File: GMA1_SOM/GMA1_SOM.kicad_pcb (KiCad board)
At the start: 6 copper layers, 67.6 x 25.4 mm, 8 parts, among them J1 USB4105-GF-A, J2 SODIMM-200_Split, U1 CCGM1A1, U2 RP2040, U3 LAN8742A-CZ-TR, U4 LAN8742A-CZ-TR, Y1 SG-210STF 25.0000ML0, Y2 SG-210STF 25.0000ML0

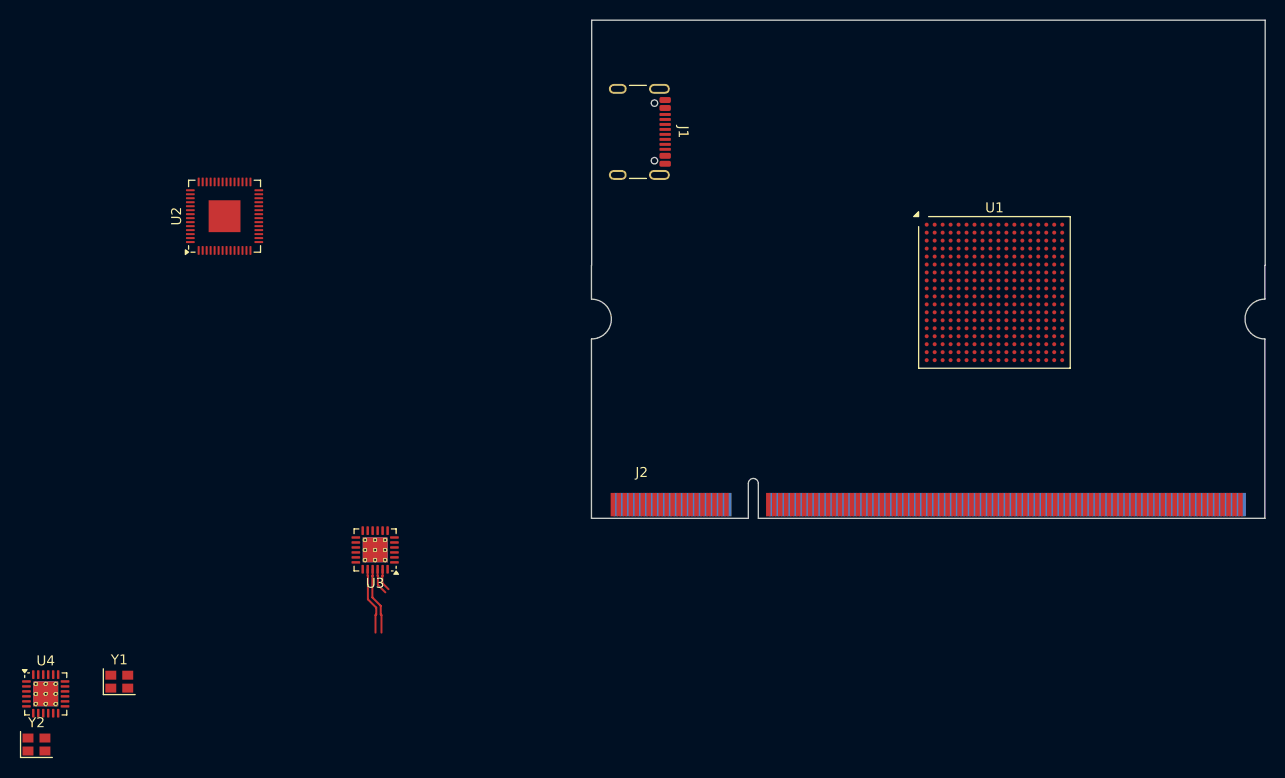
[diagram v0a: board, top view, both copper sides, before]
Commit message: add display and ram
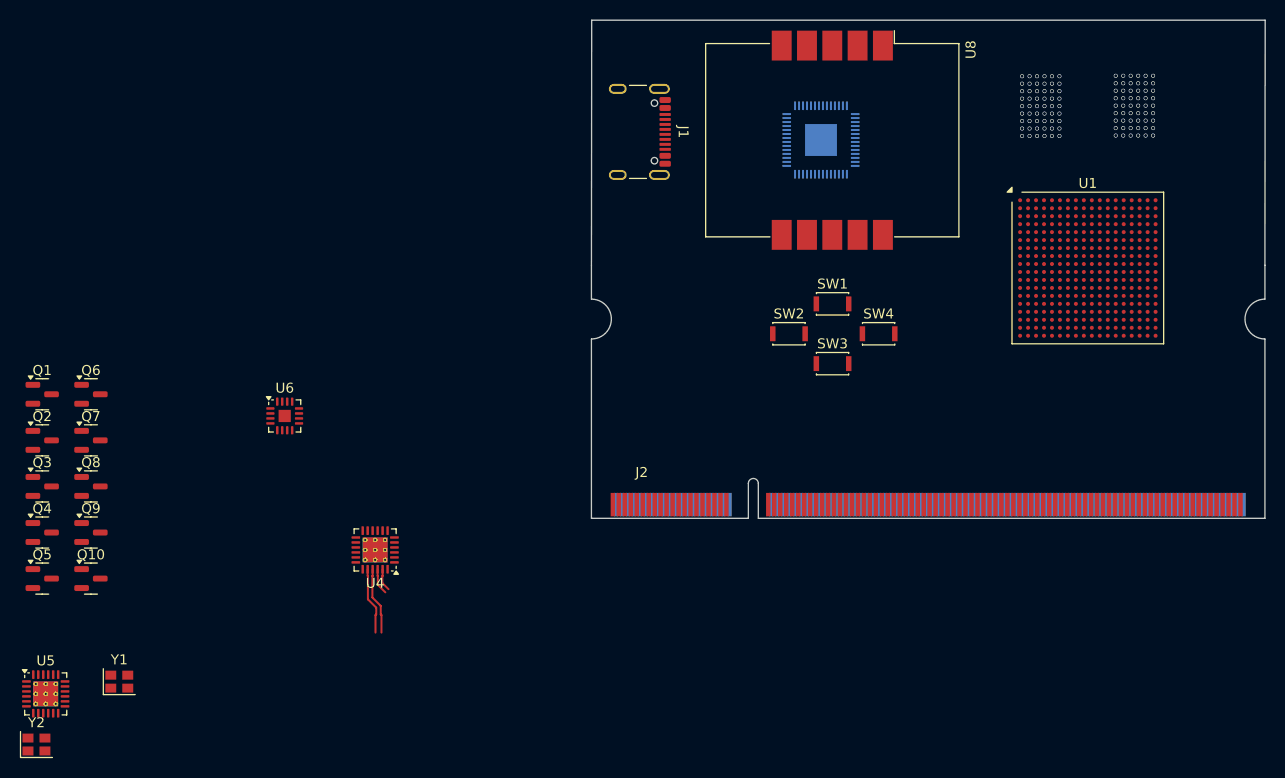
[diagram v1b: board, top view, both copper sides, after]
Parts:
- added Q1: BSS138, Package_TO_SOT_SMD:SOT-23, F.Cu at (135.0, 121.1)
- added Q10: BSS138, Package_TO_SOT_SMD:SOT-23, F.Cu at (139.9, 139.6)
- added Q2: BSS138, Package_TO_SOT_SMD:SOT-23, F.Cu at (135.0, 125.7)
- added Q3: BSS138, Package_TO_SOT_SMD:SOT-23, F.Cu at (135.0, 130.3)
- added Q4: BSS138, Package_TO_SOT_SMD:SOT-23, F.Cu at (135.0, 134.9)
- added Q5: BSS138, Package_TO_SOT_SMD:SOT-23, F.Cu at (135.0, 139.6)
- added Q6: BSS138, Package_TO_SOT_SMD:SOT-23, F.Cu at (139.9, 121.1)
- added Q7: BSS138, Package_TO_SOT_SMD:SOT-23, F.Cu at (139.9, 125.7)
- added Q8: BSS138, Package_TO_SOT_SMD:SOT-23, F.Cu at (139.9, 130.3)
- added Q9: BSS138, Package_TO_SOT_SMD:SOT-23, F.Cu at (139.9, 134.9)
- added SW1: KXT 331 LHS, Button_Switch_SMD:SW_SPST_CK_KXT3, F.Cu at (214.4, 112.0)
- added SW2: KXT 331 LHS, Button_Switch_SMD:SW_SPST_CK_KXT3, F.Cu at (210.0, 115.0)
- added SW3: KXT 331 LHS, Button_Switch_SMD:SW_SPST_CK_KXT3, F.Cu at (214.4, 118.0)
- added SW4: KXT 331 LHS, Button_Switch_SMD:SW_SPST_CK_KXT3, F.Cu at (219.0, 115.0)
- added U3: IS66WVC2M16EALL-7010BLI, Project_Library:BGA-54_6x9_6.0x8.0mm, B.Cu at (235.3, 92.2)
- added U6: MAX98357B, Package_DFN_QFN:TQFN-16-1EP_3x3mm_P0.5mm_EP1.23x1.23mm, F.Cu at (159.4, 123.2)
- added U7: IS66WVC2M16EALL-7010BLI, Project_Library:BGA-54_6x9_6.0x8.0mm, B.Cu at (244.7, 92.1)
- added U8: HDSM-543B, Display:HDSM-541B_HDSM-543B, F.Cu at (214.3, 95.6)
- U2: moved to B.Cu
- moved U2 60.3 mm to (213.2, 95.5), turned to -90 degrees
- moved U1 9.69 mm to (240.0, 108.4)
- renumbered U3 to U4, U4 to U5
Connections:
- J1 pad A1: Net-(J1-GND-PadA1) -> GND
- J1 pad A12: Net-(J1-GND-PadA1) -> GND
- J1 pad A5: unconnected-(J1-CC1-PadA5) -> Net-(J1-CC1)
- J1 pad B1: Net-(J1-GND-PadA1) -> GND
- J1 pad B12: Net-(J1-GND-PadA1) -> GND
- J1 pad B5: unconnected-(J1-CC2-PadB5) -> Net-(J1-CC2)
- J1 pad S1: unconnected-(J1-SHIELD-PadS1) -> Net-(J1-SHIELD)
- U1 pad A1: Net-(U1G-GND-PadA1) -> GND
- U1 pad A10: Net-(U1G-GND-PadA1) -> GND
- U1 pad A11: unconnected-(U1C-IO_NB_B2-PadA11) -> /Root/FPGA/A5
- U1 pad A12: unconnected-(U1C-IO_NB_B4-PadA12) -> /Root/FPGA/A9
- U1 pad A13: Net-(U1G-GND-PadA1) -> GND
- U1 pad A14: unconnected-(U1C-IO_NB_B7-PadA14) -> /Root/FPGA/A15
- U1 pad A18: Net-(U1G-GND-PadA1) -> GND
- U1 pad A3: unconnected-(U1C-IO_NA_A0-PadA3) -> /Root/FPGA/DQ1
- U1 pad A4: unconnected-(U1C-IO_NA_A1-PadA4) -> /Root/FPGA/DQ3
- U1 pad A6: unconnected-(U1C-IO_NA_A4-PadA6) -> /Root/FPGA/DQ9
- U1 pad A7: Net-(U1G-GND-PadA1) -> GND
- U1 pad A8: unconnected-(U1C-IO_NA_A7-PadA8) -> /Root/FPGA/DQ15
- U1 pad A9: unconnected-(U1C-IO_NB_B0-PadA9) -> /Root/FPGA/A1
- U1 pad B11: unconnected-(U1C-IO_NB_A2-PadB11) -> /Root/FPGA/A4
- U1 pad B12: unconnected-(U1C-IO_NB_A4-PadB12) -> /Root/FPGA/A8
- U1 pad B14: unconnected-(U1C-IO_NB_A7-PadB14) -> /Root/FPGA/A14
- U1 pad B16: Net-(U1G-GND-PadA1) -> GND
- U1 pad B3: unconnected-(U1C-IO_NA_B0-PadB3) -> /Root/FPGA/DQ2
- U1 pad B4: unconnected-(U1C-IO_NA_B1-PadB4) -> /Root/FPGA/DQ4
- U1 pad B5: unconnected-(U1C-IO_NA_A2-PadB5) -> /Root/FPGA/DQ5
- U1 pad B6: unconnected-(U1C-IO_NA_B4-PadB6) -> /Root/FPGA/DQ10
- U1 pad B8: unconnected-(U1C-IO_NA_B7-PadB8) -> /Root/FPGA/A20
- U1 pad B9: unconnected-(U1C-IO_NB_A0-PadB9) -> /Root/FPGA/A0
- U1 pad C1: Net-(U1G-GND-PadA1) -> GND
- U1 pad C10: unconnected-(U1C-IO_NB_B1-PadC10) -> /Root/FPGA/A3
- U1 pad C11: unconnected-(U1C-IO_NB_B3-PadC11) -> /Root/FPGA/A7
- U1 pad C12: unconnected-(U1C-IO_NB_B5-PadC12) -> /Root/FPGA/A11
- U1 pad C13: unconnected-(U1C-IO_NB_B6-PadC13) -> /Root/FPGA/A13
- U1 pad C14: unconnected-(U1C-IO_NB_B8-PadC14) -> /Root/FPGA/A17
- U1 pad C5: unconnected-(U1C-IO_NA_B2-PadC5) -> /Root/FPGA/DQ6
- U1 pad C6: unconnected-(U1C-IO_NA_A3-PadC6) -> /Root/FPGA/DQ7
- U1 pad C7: unconnected-(U1C-IO_NA_A5-PadC7) -> /Root/FPGA/DQ11
- U1 pad C8: unconnected-(U1C-IO_NA_A6-PadC8) -> /Root/FPGA/DQ13
- U1 pad C9: unconnected-(U1C-IO_NA_A8-PadC9) -> /Root/FPGA/A19
- U1 pad D10: unconnected-(U1C-IO_NB_A1-PadD10) -> /Root/FPGA/A2
- U1 pad D11: unconnected-(U1C-IO_NB_A3-PadD11) -> /Root/FPGA/A6
- U1 pad D12: unconnected-(U1C-IO_NB_A5-PadD12) -> /Root/FPGA/A10
- U1 pad D13: unconnected-(U1C-IO_NB_A6-PadD13) -> /Root/FPGA/A12
- U1 pad D14: unconnected-(U1C-IO_NB_A8-PadD14) -> /Root/FPGA/A16
- U1 pad D6: unconnected-(U1C-IO_NA_B3-PadD6) -> /Root/FPGA/DQ8
- U1 pad D7: unconnected-(U1C-IO_NA_B5-PadD7) -> /Root/FPGA/DQ12
- U1 pad D8: unconnected-(U1C-IO_NA_B6-PadD8) -> /Root/FPGA/DQ14
- U1 pad D9: unconnected-(U1C-IO_NA_B8-PadD9) -> /Root/FPGA/A18
- U1 pad E11: Net-(U1G-GND-PadA1) -> GND
- U1 pad E13: Net-(U1G-GND-PadA1) -> GND
- U1 pad E18: Net-(U1G-GND-PadA1) -> GND
- U1 pad E5: Net-(U1G-GND-PadA1) -> GND
- U1 pad E7: Net-(U1G-GND-PadA1) -> GND
- U1 pad E9: Net-(U1G-GND-PadA1) -> GND
- U1 pad F1: Net-(U1G-GND-PadA1) -> GND
- U1 pad F10: Net-(U1G-GND-PadA1) -> GND
- U1 pad F12: Net-(U1G-GND-PadA1) -> GND
- U1 pad F14: Net-(U1G-GND-PadA1) -> GND
- U1 pad F6: Net-(U1G-GND-PadA1) -> GND
- U1 pad F8: Net-(U1G-GND-PadA1) -> GND
- U1 pad G11: Net-(U1G-GND-PadA1) -> GND
- U1 pad G13: Net-(U1G-GND-PadA1) -> GND
- U1 pad G15: unconnected-(U1D-IO_EA_B8-PadG15) -> /Root/FPGA/DQ0
- U1 pad G16: unconnected-(U1D-IO_EA_A8-PadG16) -> /Root/FPGA/CLK
- U1 pad G17: unconnected-(U1D-IO_EA_B7-PadG17) -> /Root/FPGA/~{ADV}
- U1 pad G18: unconnected-(U1D-IO_EA_A7-PadG18) -> /Root/FPGA/~{WE}
- U1 pad G5: Net-(U1G-GND-PadA1) -> GND
- U1 pad G7: Net-(U1G-GND-PadA1) -> GND
- U1 pad G9: Net-(U1G-GND-PadA1) -> GND
- U1 pad H10: Net-(U1G-GND-PadA1) -> GND
- U1 pad H12: Net-(U1G-GND-PadA1) -> GND
- U1 pad H14: Net-(U1G-GND-PadA1) -> GND
- U1 pad H15: unconnected-(U1D-IO_EA_B6-PadH15) -> /Root/FPGA/~{CE}
- U1 pad H16: unconnected-(U1D-IO_EA_A6-PadH16) -> /Root/FPGA/~{UB}
- U1 pad H18: Net-(U1G-GND-PadA1) -> GND
- U1 pad H6: Net-(U1G-GND-PadA1) -> GND
- U1 pad H8: Net-(U1G-GND-PadA1) -> GND
- U1 pad J1: Net-(U1G-GND-PadA1) -> GND
- U1 pad J11: Net-(U1G-GND-PadA1) -> GND
- U1 pad J13: Net-(U1G-GND-PadA1) -> GND
- U1 pad J15: unconnected-(U1D-IO_EA_B5-PadJ15) -> /Root/FPGA/~{LB}
- U1 pad J16: unconnected-(U1D-IO_EA_A5-PadJ16) -> /Root/FPGA/CRE
- U1 pad J17: unconnected-(U1D-IO_EA_B4-PadJ17) -> /Root/FPGA/~{OE}
- U1 pad J18: unconnected-(U1D-IO_EA_A4-PadJ18) -> /Root/FPGA/WAIT0
- U1 pad J5: Net-(U1G-GND-PadA1) -> GND
- U1 pad J7: Net-(U1G-GND-PadA1) -> GND
- U1 pad J9: Net-(U1G-GND-PadA1) -> GND
- U1 pad K10: Net-(U1G-GND-PadA1) -> GND
- U1 pad K12: Net-(U1G-GND-PadA1) -> GND
- U1 pad K14: Net-(U1G-GND-PadA1) -> GND
- U1 pad K15: unconnected-(U1D-IO_EA_B3-PadK15) -> /Root/FPGA/WAIT1
- U1 pad K6: Net-(U1G-GND-PadA1) -> GND
- U1 pad K8: Net-(U1G-GND-PadA1) -> GND
- U1 pad L1: unconnected-(U1F-IO_WB_A3-PadL1) -> /Root/FPGA/IO_WB_A3
- U1 pad L11: Net-(U1G-GND-PadA1) -> GND
- U1 pad L13: Net-(U1G-GND-PadA1) -> GND
- U1 pad L18: Net-(U1G-GND-PadA1) -> GND
- U1 pad L2: unconnected-(U1F-IO_WB_B3-PadL2) -> /Root/FPGA/IO_WB_B3
- U1 pad L3: unconnected-(U1F-IO_WB_A2-PadL3) -> /Root/FPGA/IO_WB_A2
- U1 pad L4: unconnected-(U1F-IO_WB_B2-PadL4) -> /Root/FPGA/IO_WB_B2
- U1 pad L5: Net-(U1G-GND-PadA1) -> GND
- U1 pad L7: Net-(U1G-GND-PadA1) -> GND
- U1 pad L9: Net-(U1G-GND-PadA1) -> GND
- U1 pad M1: Net-(U1G-GND-PadA1) -> GND
- U1 pad M10: Net-(U1G-GND-PadA1) -> GND
- U1 pad M12: Net-(U1G-GND-PadA1) -> GND
- U1 pad M16: Net-(U1G-GND-PadA1) -> GND
- U1 pad M6: Net-(U1G-GND-PadA1) -> GND
- U1 pad M8: Net-(U1G-GND-PadA1) -> GND
- U1 pad N12: Net-(U1G-GND-PadA1) -> GND
- U1 pad N17: Net-(U1G-GND-PadA1) -> GND
- U1 pad N7: Net-(U1G-GND-PadA1) -> GND
- U1 pad N9: Net-(U1G-GND-PadA1) -> GND
- U1 pad P4: Net-(U1G-GND-PadA1) -> GND
- U1 pad P7: Net-(U1G-GND-PadA1) -> GND
- U1 pad P9: Net-(U1G-GND-PadA1) -> GND
- U1 pad R12: Net-(U1G-GND-PadA1) -> GND
- U1 pad R16: Net-(U1G-GND-PadA1) -> GND
- U1 pad T11: Net-(U1G-GND-PadA1) -> GND
- U1 pad T17: Net-(U1G-GND-PadA1) -> GND
- U1 pad T4: Net-(U1G-GND-PadA1) -> GND
- U1 pad U14: Net-(U1G-GND-PadA1) -> GND
- U1 pad U15: Net-(U1G-GND-PadA1) -> GND
- U1 pad U16: Net-(U1G-GND-PadA1) -> GND
- U1 pad V1: Net-(U1G-GND-PadA1) -> GND
- U1 pad V14: Net-(U1G-GND-PadA1) -> GND
- U1 pad V16: Net-(U1G-GND-PadA1) -> GND
- U1 pad V18: Net-(U1G-GND-PadA1) -> GND
- U1 pad V6: Net-(U1G-GND-PadA1) -> GND
- U1 pad V9: Net-(U1G-GND-PadA1) -> GND
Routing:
- net unconnected-(U7-NC-PadJ6): vias 0 -> 1
- net unconnected-(U7-NC-PadJ5): vias 0 -> 1
- net unconnected-(U7-NC-PadJ4): vias 0 -> 1
- net unconnected-(U7-NC-PadE3): vias 0 -> 1
- net unconnected-(U3-NC-PadJ6): vias 0 -> 1
- net unconnected-(U3-NC-PadJ5): vias 0 -> 1
- net unconnected-(U3-NC-PadJ4): vias 0 -> 1
- net unconnected-(U3-NC-PadE3): vias 0 -> 1
- net GND: vias 0 -> 4
- net /Root/FPGA/~{WE}: vias 0 -> 2
- net /Root/FPGA/~{UB}: vias 0 -> 2
- net /Root/FPGA/~{OE}: vias 0 -> 2
- net /Root/FPGA/~{LB}: vias 0 -> 2
- net /Root/FPGA/~{CE}: vias 0 -> 2
- net /Root/FPGA/~{ADV}: vias 0 -> 2
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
